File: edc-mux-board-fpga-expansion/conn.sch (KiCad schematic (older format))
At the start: 24 parts, among them U12 P82B96, U13 TLV320AIC3206, U14 MAX4910

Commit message: Reannotating entire schematic
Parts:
- renumbered C141 to C10, C142 to C11, C143 to C12, C144 to C13, C145 to C14, C146 to C15, C147 to C16, C148 to C17, C149 to C18, C150 to C19, C151 to C20, C134 to C3, C135 to C4, C136 to C5, C137 to C6, C138 to C7, C139 to C8, C140 to C9, FB4 to FB1, R17 to R1, R18 to R2, U12 to U3, U13 to U4, U14 to U5

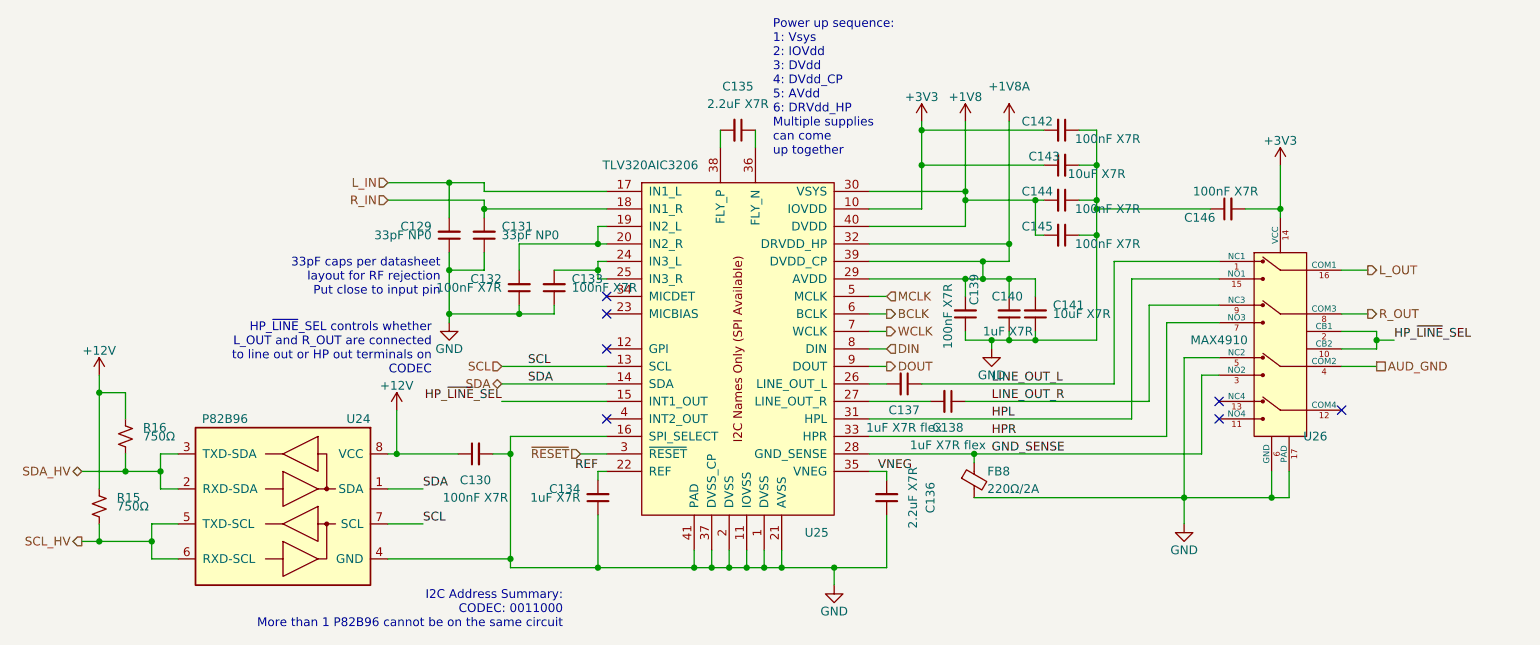
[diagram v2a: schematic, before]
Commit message: Changed to new 2:1 switch chip
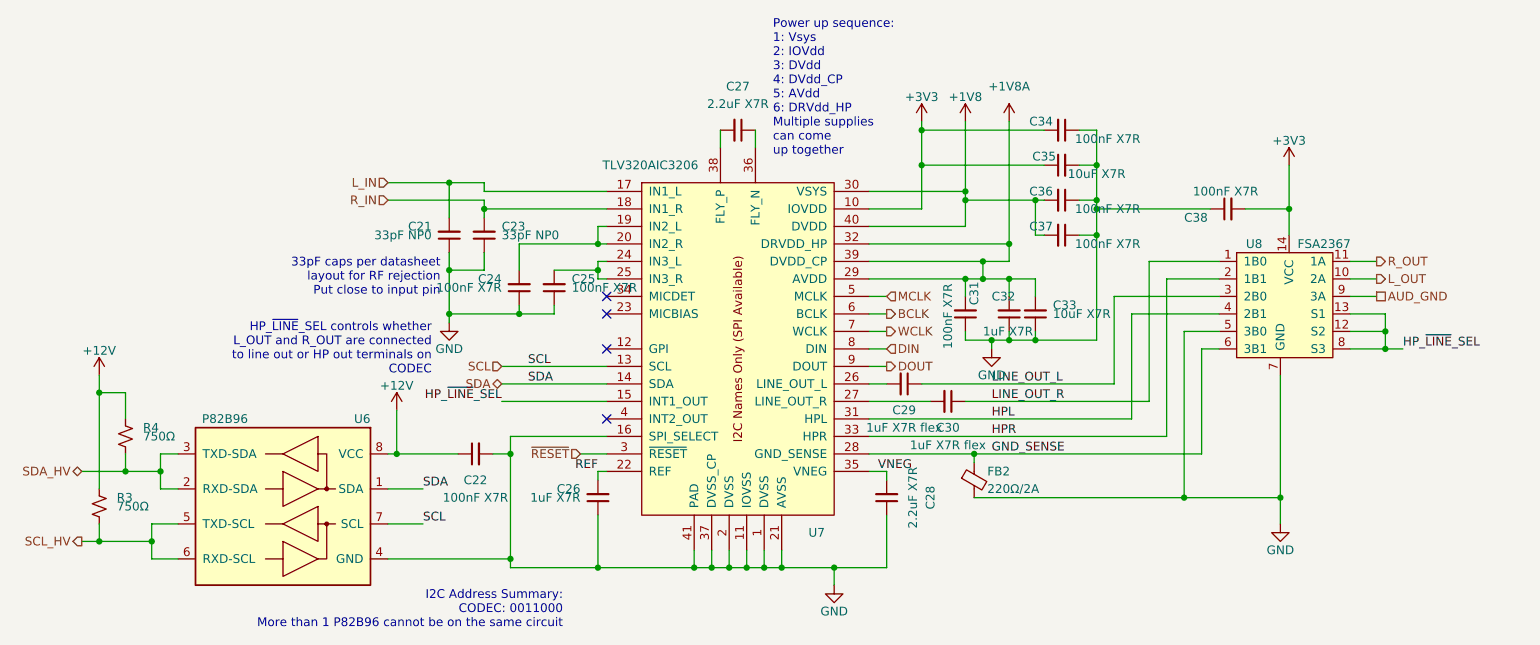
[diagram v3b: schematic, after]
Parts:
- removed U5: MAX4910, Package_DFN_QFN:TQFN-16-1EP_3x3mm_P0.5mm_EP1.23x1.23mm, symbol SW-dallas-semi-maxim:MAX4910
- added U5: FSA2367, Package_SO:TSSOP-14_4.4x5mm_P0.65mm, symbol SW-ON-Semi:FSA2367
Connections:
- net +3V3: now also U5.14 (VCC)
- net AUD_GND: now also U5.9 (3A)
- net GND: now also U5.5 (3B0), U5.7 (GND)
- net GND_SENSE: now also U5.6 (3B1)
- net HPL: now also U5.4 (2B1)
- net HPR: now also U5.2 (1B1)
- net HP_~LINE~_SEL: now also U5.12 (S2), U5.13 (S1), U5.8 (S3)
- net LINE_OUT_L: now also U5.3 (2B0)
- net LINE_OUT_R: now also U5.1 (1B0)
- net L_OUT: now also U5.10 (2A)
- net R_OUT: now also U5.11 (1A)
- no-connect marks 7 -> 4

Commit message: starting to connect expansion connector
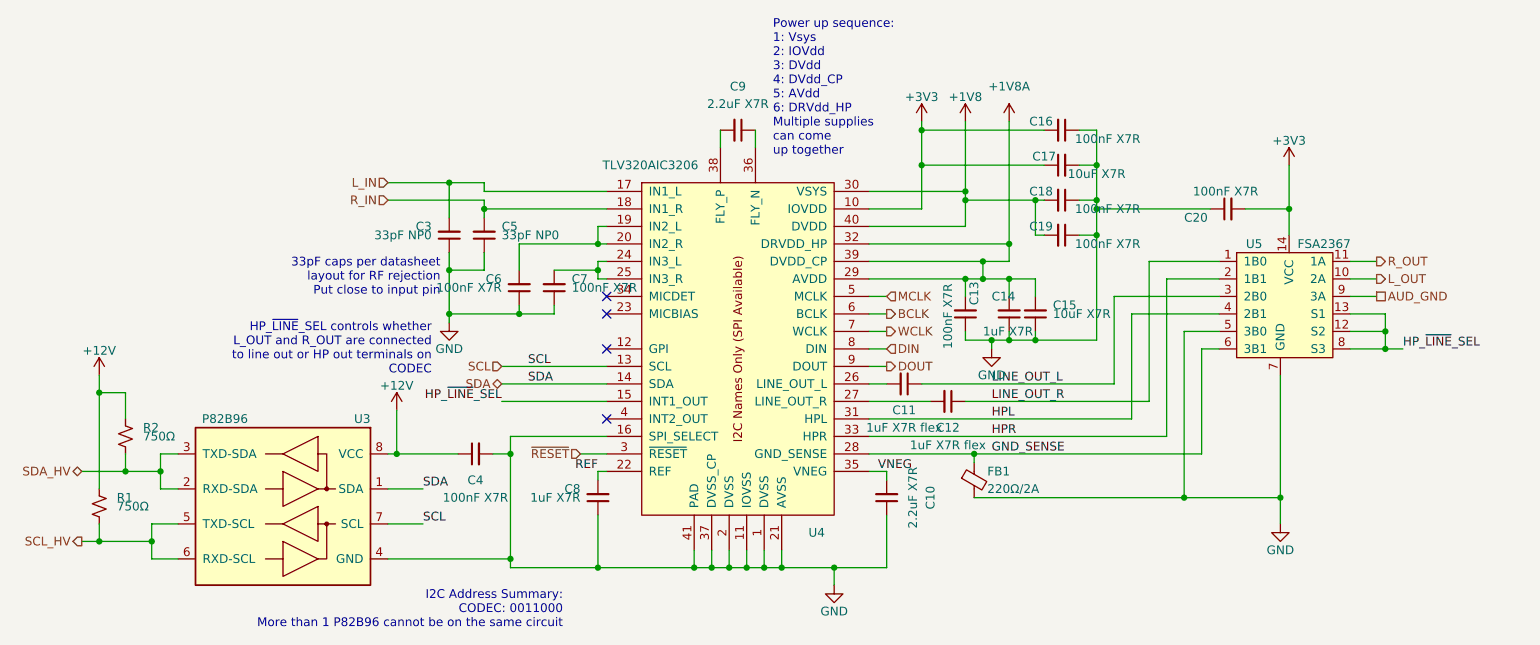
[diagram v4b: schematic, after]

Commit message: More work on expansion connector pinout connections
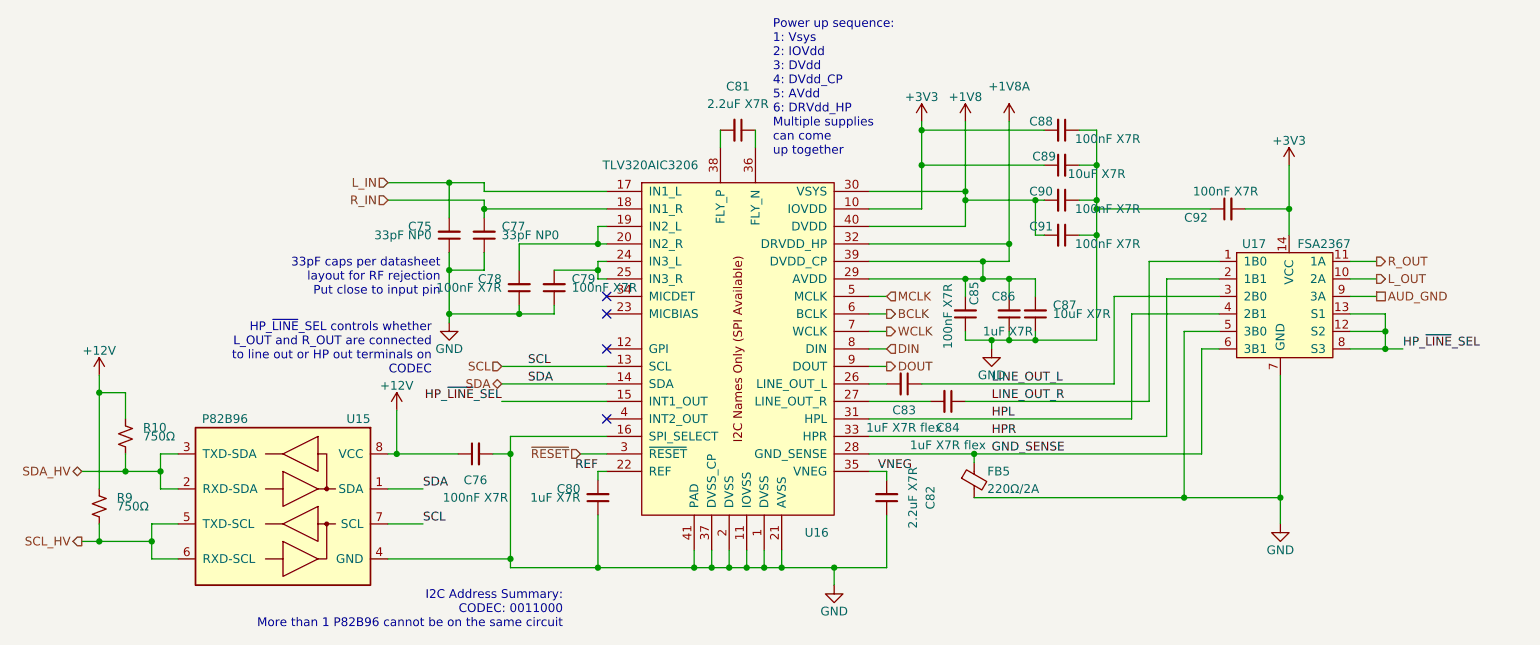
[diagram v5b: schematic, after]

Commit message: Finished routing of Expansion board. passed DRC
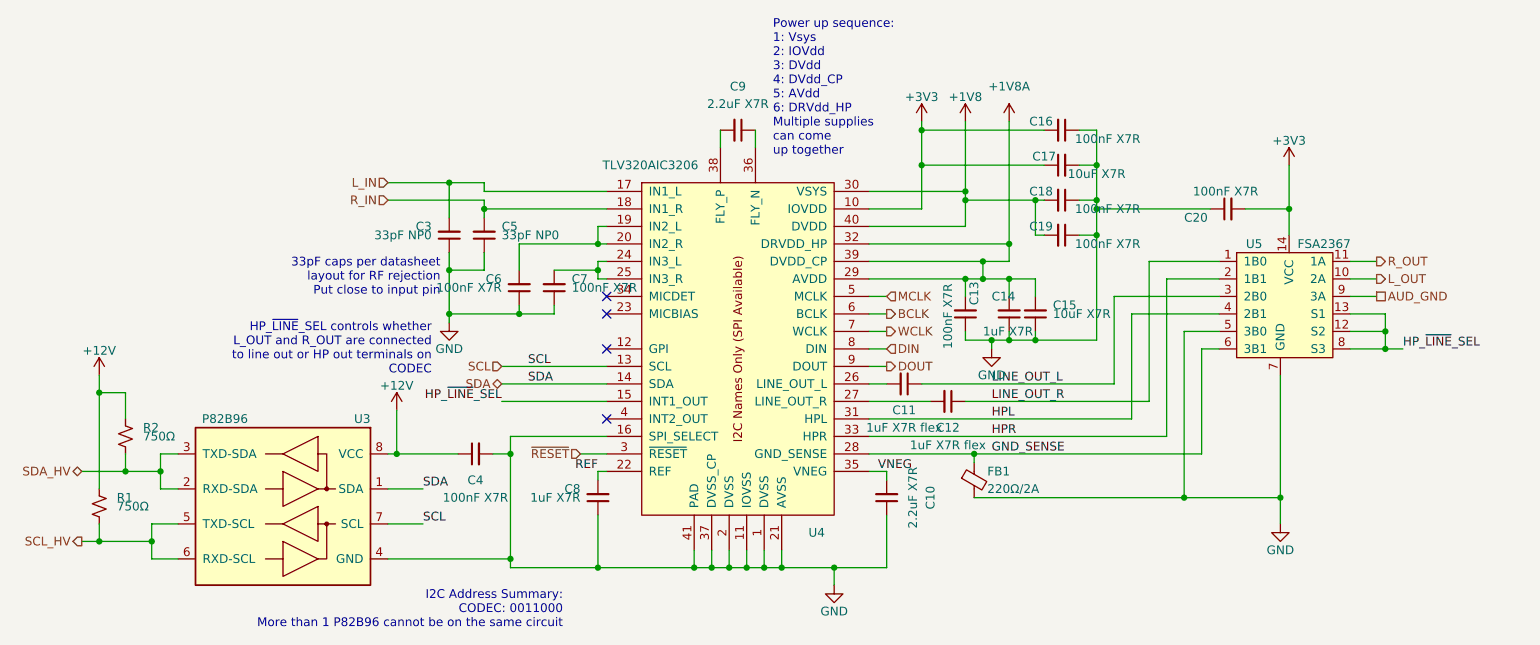
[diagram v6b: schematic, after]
